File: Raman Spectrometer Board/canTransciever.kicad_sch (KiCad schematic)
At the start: 16 parts, among them SW1 SW_Push, SW2 SW_Push, U1 ATA6561, U3 ATA6561

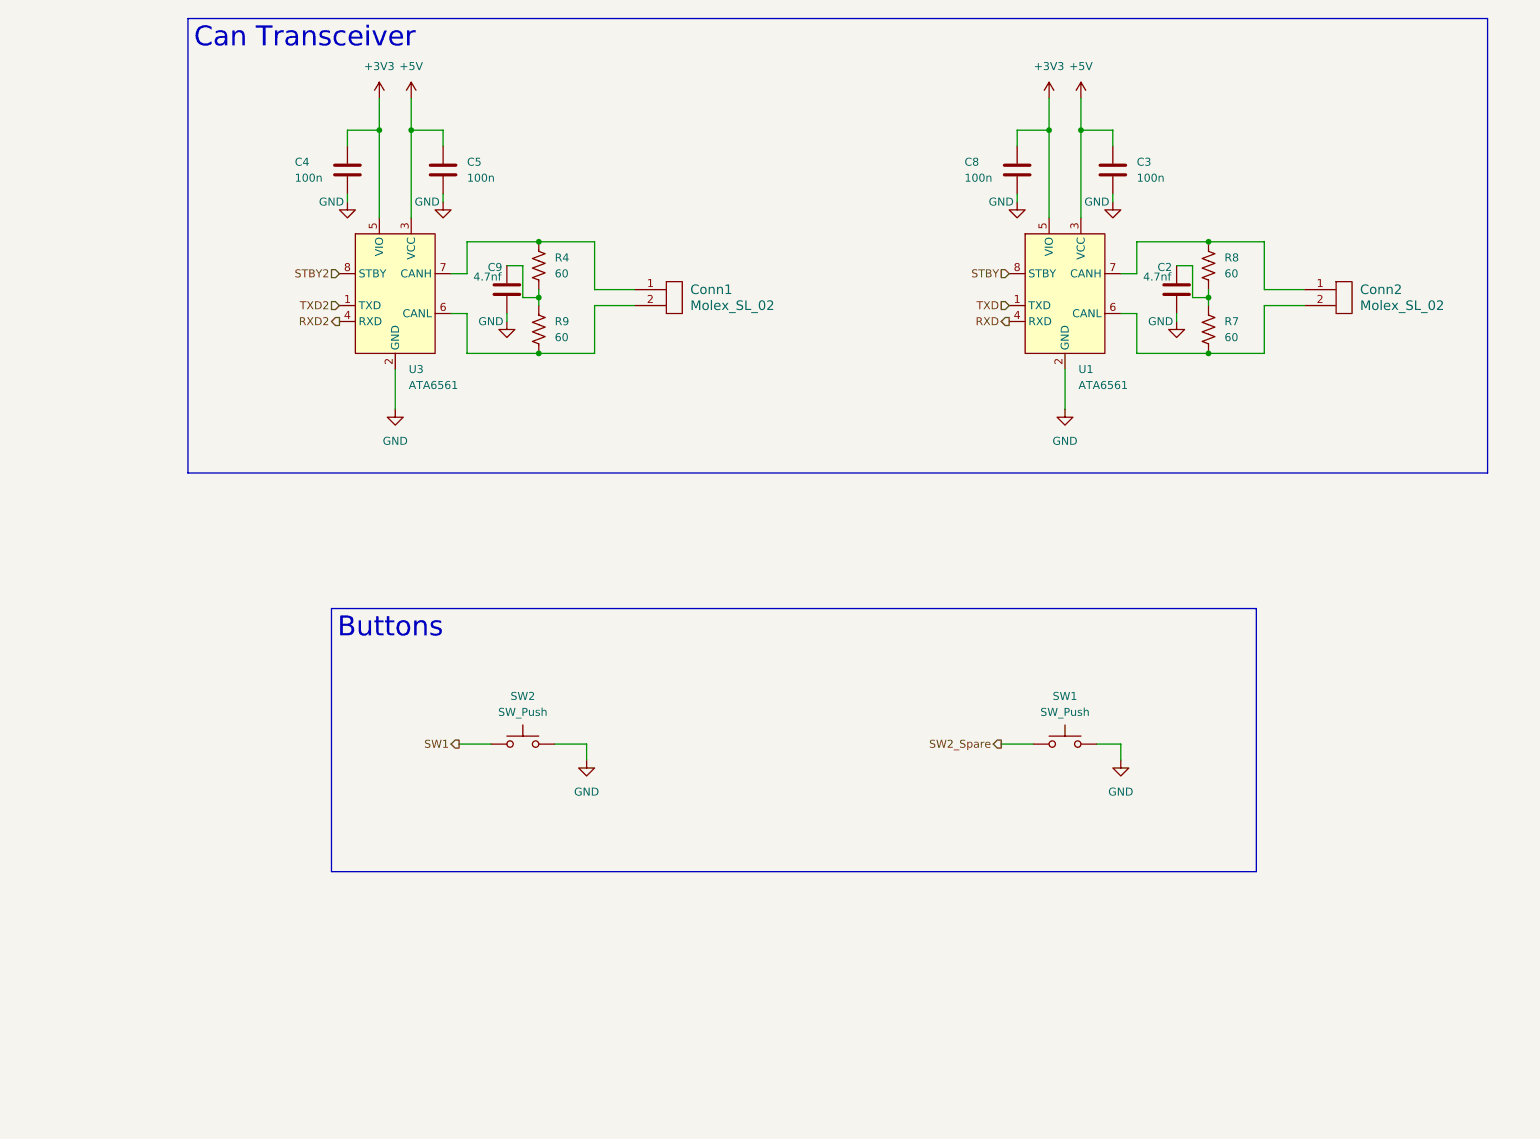
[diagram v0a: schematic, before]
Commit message: Fixed switch connections
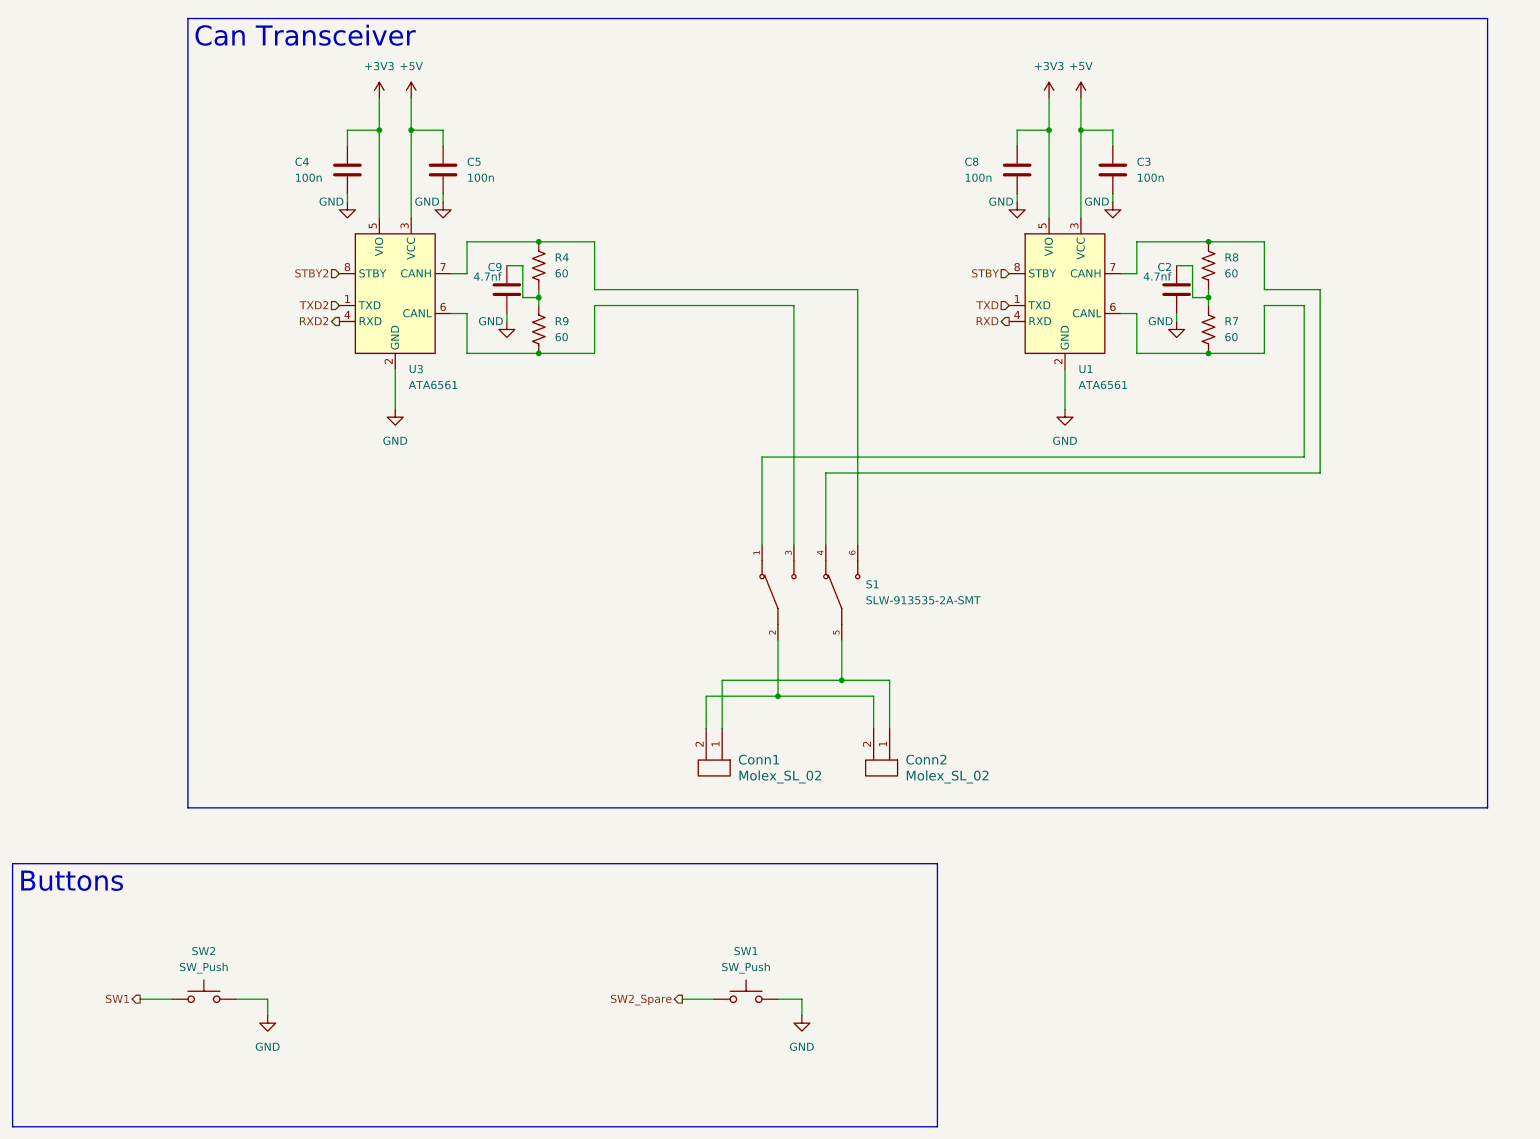
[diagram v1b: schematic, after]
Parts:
- added S1: SLW-913535-2A-SMT, MRDT_Switches:SW_SLW-913535-2A-SMT, symbol MRDT_Switches:SLW-913535-2A-SMT
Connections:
- net at R4.1, U3.7 (CANH): now also S1.6; no longer Conn1.1
- net at R9.2, U3.6 (CANL): now also S1.3; no longer Conn1.2
- net at R7.2, U1.6 (CANL): now also S1.1; no longer Conn2.2
- net at R8.1, U1.7 (CANH): now also S1.4; no longer Conn2.1
- new net: Conn1.2, Conn2.2, S1.2
- new net: Conn1.1, Conn2.1, S1.5
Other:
- moved on the sheet: Conn1, Conn2, SW1, SW2

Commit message: PCB final design? maybe
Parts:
- S1: footprint MRDT_Switches:SW_SLW-913535-2A-SMT -> Raman:SW_SLW-913535-2A-SMT
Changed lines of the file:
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@@
 			)
 		)
-		(property "Footprint" "MRDT_Switches:SW_SLW-913535-2A-SMT"
+		(property "Footprint" "Raman:SW_SLW-913535-2A-SMT"
 			(at 149.86 110.49 0)
 			(effects

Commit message: Added laser driver sheet
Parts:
- renumbered C4 to C12, C5 to C13, C9 to C14, C8 to C15, C3 to C16, C2 to C17, Conn1 to Conn6, Conn2 to Conn7, R4 to R25, R9 to R26, R8 to R27, R7 to R28, SW1 to SW3, U3 to U5, U1 to U6
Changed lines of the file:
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@@
 		(dnp no)
 		(fields_autoplaced yes)
-		(property "Reference" "#PWR016"
+		(property "Reference" "#PWR051"
 			(at 86.36 35.56 0)
 			(effects
@@
 			(project "RamanSpectrometerBoard"
 				(path "/ab487c59-f066-48f5-a383-99e8eaf806bf/2495d964-2266-4066-961c-06fbcb7a3cda"
-					(reference "#PWR016")
+					(reference "#PWR051")
 					(unit 1)
 				)
@@
 		(dnp no)
 		(fields_autoplaced yes)
-		(property "Reference" "#PWR03"
+		(property "Reference" "#PWR057"
 			(at 190.5 87.63 0)
 			(effects
@@
 			(project "RamanSpectrometerBoard"
 				(path "/ab487c59-f066-48f5-a383-99e8eaf806bf/2495d964-2266-4066-961c-06fbcb7a3cda"
-					(reference "#PWR03")
+					(reference "#PWR057")
 					(unit 1)
 				)
@@
 		(on_board yes)
 		(dnp no)
-		(property "Reference" "C9"
+		(property "Reference" "C14"
 			(at 98.552 58.674 0)
 			(effects
@@
 			(project "RamanSpectrometerBoard"
 				(path "/ab487c59-f066-48f5-a383-99e8eaf806bf/2495d964-2266-4066-961c-06fbcb7a3cda"
-					(reference "C9")
+					(reference "C14")
 					(unit 1)
 				)
@@
 		(dnp no)
 		(fields_autoplaced yes)
-		(property "Reference" "R4"
+		(property "Reference" "R25"
 			(at 109.22 57.1499 0)
 			(effects
@@
 			(project "RamanSpectrometerBoard"
 				(path "/ab487c59-f066-48f5-a383-99e8eaf806bf/2495d964-2266-4066-961c-06fbcb7a3cda"
-					(reference "R4")
+					(reference "R25")
 					(unit 1)
 				)
@@
 		(on_board yes)
 		(dnp no)
-		(property "Reference" "C4"
+		(property "Reference" "C12"
 			(at 67.818 41.91 0)
 			(effects
@@
 			(project "RamanSpectrometerBoard"
 				(path "/ab487c59-f066-48f5-a383-99e8eaf806bf/2495d964-2266-4066-961c-06fbcb7a3cda"
-					(reference "C4")
+					(reference "C12")
 					(unit 1)
 				)
@@
 		(dnp no)
 		(fields_autoplaced yes)
-		(property "Reference" "#PWR014"
+		(property "Reference" "#PWR049"
 			(at 81.28 35.56 0)
 			(effects
@@
 			(project "RamanSpectrometerBoard"
 				(path "/ab487c59-f066-48f5-a383-99e8eaf806bf/2495d964-2266-4066-961c-06fbcb7a3cda"
-					(reference "#PWR014")
+					(reference "#PWR049")
 					(unit 1)
 				)
@@
 		(dnp no)
 		(fields_autoplaced yes)
-		(property "Reference" "Conn1"
+		(property "Reference" "Conn6"
 			(at 138.43 137.1599 90)
 			(effects
@@
 			(project "RamanSpectrometerBoard"
 				(path "/ab487c59-f066-48f5-a383-99e8eaf806bf/2495d964-2266-4066-961c-06fbcb7a3cda"
-					(reference "Conn1")
+					(reference "Conn6")
 					(unit 1)
 				)
@@
 		(on_board yes)
 		(dnp no)
-		(property "Reference" "#PWR02"
+		(property "Reference" "#PWR060"
 			(at 208.28 73.66 0)
 			(effects
@@
 			(project "RamanSpectrometerBoard"
 				(path "/ab487c59-f066-48f5-a383-99e8eaf806bf/2495d964-2266-4066-961c-06fbcb7a3cda"
-					(reference "#PWR02")
+					(reference "#PWR060")
 					(unit 1)
 				)
@@
 		(dnp no)
 		(fields_autoplaced yes)
-		(property "Reference" "#PWR015"
+		(property "Reference" "#PWR050"
 			(at 83.82 87.63 0)
 			(effects
@@
 			(project "RamanSpectrometerBoard"
 				(path "/ab487c59-f066-48f5-a383-99e8eaf806bf/2495d964-2266-4066-961c-06fbcb7a3cda"
-					(reference "#PWR015")
+					(reference "#PWR050")
 					(unit 1)
 				)
@@
 		(on_board yes)
 		(dnp no)
-		(property "Reference" "#PWR013"
+		(property "Reference" "#PWR048"
 			(at 76.2 54.61 0)
 			(effects
@@
 			(project "RamanSpectrometerBoard"
 				(path "/ab487c59-f066-48f5-a383-99e8eaf806bf/2495d964-2266-4066-961c-06fbcb7a3cda"
-					(reference "#PWR013")
+					(reference "#PWR048")
 					(unit 1)
 				)
@@
 		(on_board yes)
 		(dnp no)
-		(property "Reference" "#PWR035"
+		(property "Reference" "#PWR055"
 			(at 182.88 54.61 0)
 			(effects
@@
 			(project "RamanSpectrometerBoard"
 				(path "/ab487c59-f066-48f5-a383-99e8eaf806bf/2495d964-2266-4066-961c-06fbcb7a3cda"
-					(reference "#PWR035")
+					(reference "#PWR055")
 					(unit 1)
 				)
@@
 		(on_board yes)
 		(dnp no)
-		(property "Reference" "#PWR017"
+		(property "Reference" "#PWR059"
 			(at 198.12 54.61 0)
 			(effects
@@
 			(project "RamanSpectrometerBoard"
 				(path "/ab487c59-f066-48f5-a383-99e8eaf806bf/2495d964-2266-4066-961c-06fbcb7a3cda"
-					(reference "#PWR017")
+					(reference "#PWR059")
 					(unit 1)
 				)
@@
 		(dnp no)
 		(fields_autoplaced yes)
-		(property "Reference" "R7"
+		(property "Reference" "R28"
 			(at 215.9 67.3099 0)
 			(effects
@@
 			(project "RamanSpectrometerBoard"
 				(path "/ab487c59-f066-48f5-a383-99e8eaf806bf/2495d964-2266-4066-961c-06fbcb7a3cda"
-					(reference "R7")
+					(reference "R28")
 					(unit 1)
 				)
@@
 		(dnp no)
 		(fields_autoplaced yes)
-		(property "Reference" "C5"
+		(property "Reference" "C13"
 			(at 95.25 41.9099 0)
 			(effects
@@
 			(project "RamanSpectrometerBoard"
 				(path "/ab487c59-f066-48f5-a383-99e8eaf806bf/2495d964-2266-4066-961c-06fbcb7a3cda"
-					(reference "C5")
+					(reference "C13")
 					(unit 1)
 				)
@@
 		(on_board yes)
 		(dnp no)
-		(property "Reference" "#PWR036"
+		(property "Reference" "#PWR052"
 			(at 91.44 54.61 0)
 			(effects
@@
 			(project "RamanSpectrometerBoard"
 				(path "/ab487c59-f066-48f5-a383-99e8eaf806bf/2495d964-2266-4066-961c-06fbcb7a3cda"
-					(reference "#PWR036")
+					(reference "#PWR052")
 					(unit 1)
 				)
@@
 		(dnp no)
 		(fields_autoplaced yes)
-		(property "Reference" "Conn2"
+		(property "Reference" "Conn7"
 			(at 165.1 137.1599 90)
 			(effects
@@
 			(project "RamanSpectrometerBoard"
 				(path "/ab487c59-f066-48f5-a383-99e8eaf806bf/2495d964-2266-4066-961c-06fbcb7a3cda"
-					(reference "Conn2")
+					(reference "Conn7")
 					(unit 1)
 				)
@@
 		(dnp no)
 		(fields_autoplaced yes)
-		(property "Reference" "U1"
+		(property "Reference" "U6"
 			(at 192.6433 74.93 0)
 			(effects
@@
 			(project ""
 				(path "/ab487c59-f066-48f5-a383-99e8eaf806bf/2495d964-2266-4066-961c-06fbcb7a3cda"
-					(reference "U1")
+					(reference "U6")
 					(unit 1)
 				)
@@
 		(on_board yes)
 		(dnp no)
-		(property "Reference" "#PWR037"
+		(property "Reference" "#PWR053"
 			(at 101.6 73.66 0)
 			(effects
@@
 			(project "RamanSpectrometerBoard"
 				(path "/ab487c59-f066-48f5-a383-99e8eaf806bf/2495d964-2266-4066-961c-06fbcb7a3cda"
-					(reference "#PWR037")
+					(reference "#PWR053")
 					(unit 1)
 				)
@@
 		(dnp no)
 		(fields_autoplaced yes)
-		(property "Reference" "C3"
+		(property "Reference" "C16"
 			(at 201.93 41.9099 0)
 			(effects
@@
 			(project "RamanSpectrometerBoard"
 				(path "/ab487c59-f066-48f5-a383-99e8eaf806bf/2495d964-2266-4066-961c-06fbcb7a3cda"
-					(reference "C3")
+					(reference "C16")
 					(unit 1)
 				)
@@
 		(on_board yes)
 		(dnp no)
-		(property "Reference" "C8"
+		(property "Reference" "C15"
 			(at 174.498 41.91 0)
 			(effects
@@
 			(project "RamanSpectrometerBoard"
 				(path "/ab487c59-f066-48f5-a383-99e8eaf806bf/2495d964-2266-4066-961c-06fbcb7a3cda"
-					(reference "C8")
+					(reference "C15")
 					(unit 1)
 				)
@@
 		(dnp no)
 		(fields_autoplaced yes)
-		(property "Reference" "U3"
+		(property "Reference" "U5"
 			(at 85.9633 74.93 0)
 			(effects
@@
 			(project "RamanSpectrometerBoard"
 				(path "/ab487c59-f066-48f5-a383-99e8eaf806bf/2495d964-2266-4066-961c-06fbcb7a3cda"
-					(reference "U3")
+					(reference "U5")
 					(unit 1)
 				)
@@
 		(dnp no)
 		(fields_autoplaced yes)
-		(property "Reference" "#PWR050"
+		(property "Reference" "#PWR054"
 			(at 148.59 184.15 0)
 			(effects
@@
 			(project "RamanSpectrometerBoard"
 				(path "/ab487c59-f066-48f5-a383-99e8eaf806bf/2495d964-2266-4066-961c-06fbcb7a3cda"
-					(reference "#PWR050")
+					(reference "#PWR054")
 					(unit 1)
 				)
@@
 		(dnp no)
 		(fields_autoplaced yes)
-		(property "Reference" "#PWR041"
+		(property "Reference" "#PWR047"
 			(at 63.5 184.15 0)
 			(effects
@@
 			(project "RamanSpectrometerBoard"
 				(path "/ab487c59-f066-48f5-a383-99e8eaf806bf/2495d964-2266-4066-961c-06fbcb7a3cda"
-					(reference "#PWR041")
+					(reference "#PWR047")
 					(unit 1)
 				)
@@
 		(dnp no)
 		(fields_autoplaced yes)
-		(property "Reference" "R9"
+		(property "Reference" "R26"
 			(at 109.22 67.3099 0)
 			(effects
@@
 			(project "RamanSpectrometerBoard"
 				(path "/ab487c59-f066-48f5-a383-99e8eaf806bf/2495d964-2266-4066-961c-06fbcb7a3cda"
-					(reference "R9")
+					(reference "R26")
 					(unit 1)
 				)
@@
 		(dnp no)
 		(fields_autoplaced yes)
-		(property "Reference" "R8"
+		(property "Reference" "R27"
 			(at 215.9 57.1499 0)
 			(effects
@@
 			(project "RamanSpectrometerBoard"
 				(path "/ab487c59-f066-48f5-a383-99e8eaf806bf/2495d964-2266-4066-961c-06fbcb7a3cda"
-					(reference "R8")
+					(reference "R27")
 					(unit 1)
 				)
@@
 		(dnp no)
 		(fields_autoplaced yes)
-		(property "Reference" "#PWR012"
+		(property "Reference" "#PWR058"
 			(at 193.04 35.56 0)
 			(effects
@@
 			(project "RamanSpectrometerBoard"
 				(path "/ab487c59-f066-48f5-a383-99e8eaf806bf/2495d964-2266-4066-961c-06fbcb7a3cda"
-					(reference "#PWR012")
+					(reference "#PWR058")
 					(unit 1)
 				)
@@
 		(dnp no)
 		(fields_autoplaced yes)
-		(property "Reference" "SW1"
+		(property "Reference" "SW3"
 			(at 139.7 167.64 0)
 			(effects
@@
 			(project "RamanSpectrometerBoard"
 				(path "/ab487c59-f066-48f5-a383-99e8eaf806bf/2495d964-2266-4066-961c-06fbcb7a3cda"
-					(reference "SW1")
+					(reference "SW3")
 					(unit 1)
 				)
@@
 		(on_board yes)
 		(dnp no)
-		(property "Reference" "C2"
+		(property "Reference" "C17"
 			(at 205.232 58.674 0)
 			(effects
@@
 			(project "RamanSpectrometerBoard"
 				(path "/ab487c59-f066-48f5-a383-99e8eaf806bf/2495d964-2266-4066-961c-06fbcb7a3cda"
-					(reference "C2")
+					(reference "C17")
 					(unit 1)
 				)
@@
 		(dnp no)
 		(fields_autoplaced yes)
-		(property "Reference" "#PWR018"
+		(property "Reference" "#PWR056"
 			(at 187.96 35.56 0)
 			(effects
@@
 			(project "RamanSpectrometerBoard"
 				(path "/ab487c59-f066-48f5-a383-99e8eaf806bf/2495d964-2266-4066-961c-06fbcb7a3cda"
-					(reference "#PWR018")
-					(unit 1)
-				)
+					(reference "#PWR056")
+					(unit 1)
+				)
